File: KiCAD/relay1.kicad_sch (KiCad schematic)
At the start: 15 parts, among them K1 SANYOU_SRD_Form_C, K2 SANYOU_SRD_Form_C, Q2 UMH3N, Q3 MMBT3906, Q4 MMBT3906

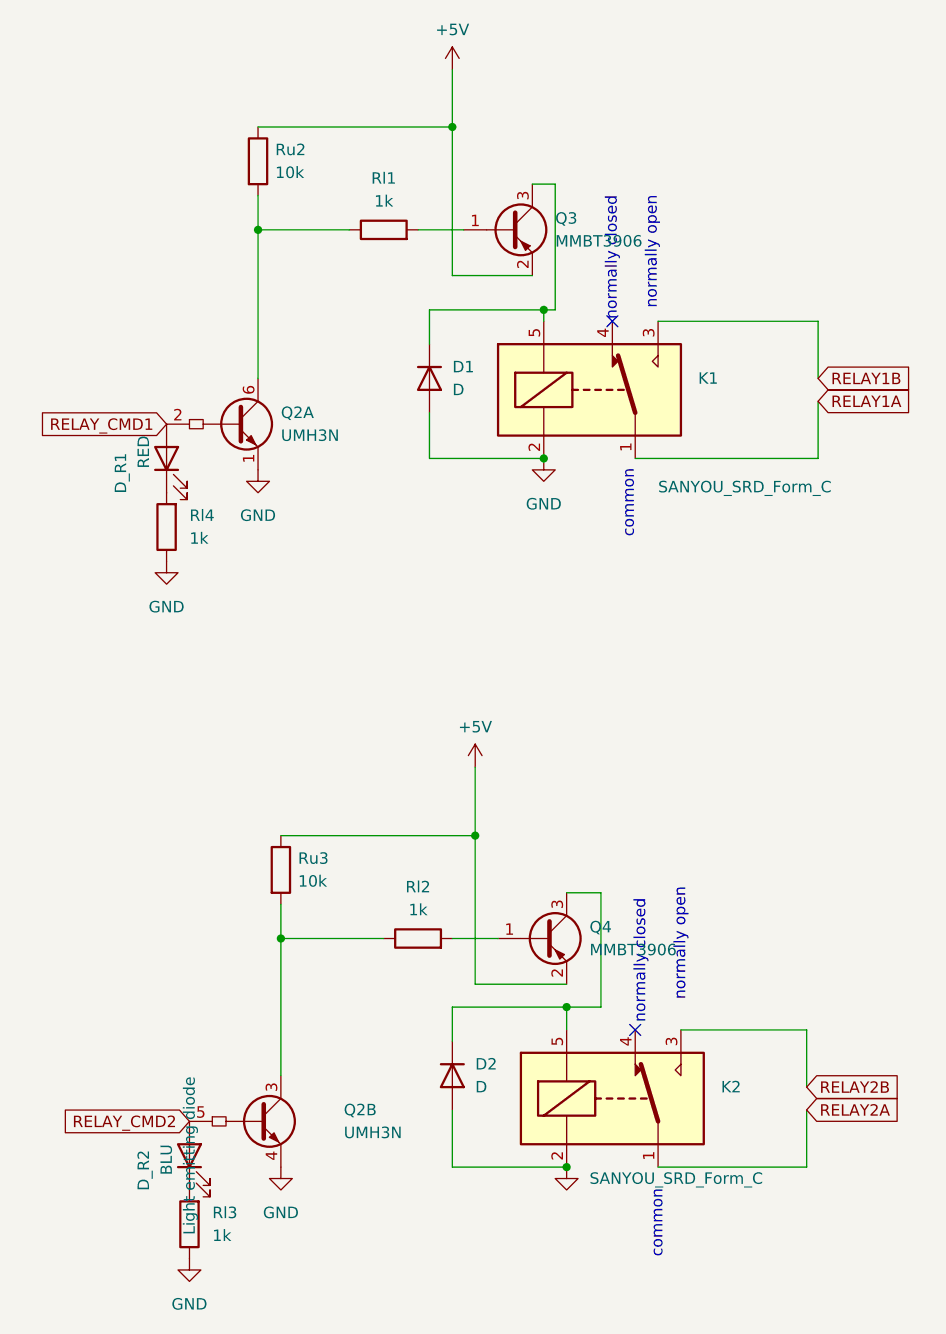
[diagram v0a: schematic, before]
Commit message: Version 2.1.0: four sonars, USB-C (#26)
## [2.1.0] - 2026-10-14

### Added
- **Hardware Board v3.1 & Enclosure Updates**: KiCAD PCB updates for
board v3.1 with revised BOM, updated 3D printable enclosure (better
SHTC3 thermal isolation, labeled connectors, improved USB-C port
clearance), and solder stencil support frame model.
- **HMM Visualization & Retraining Workflow**: Added
`analysis/hmm_to_svg.py` to generate SVG state transition diagrams from
trained HMM models, and added characterization workflow in
`analysis/retrain.py`.

### Changed
- **Sonar Watchdog & Timeout Stability**: Added sonar ping timeout
handling to prevent blocking pulses from triggering the ESP32 hardware
watchdog.

### Removed
- **Retired Legacy Hardware**: Removed firmware and PlatformIO
configuration support for legacy Classic ESP32 boards (Board v1/v2 /
`node32s`), focusing entirely on Board v3.x (ESP32-S3).

## [2.0.0] - 2026-08-21

### Added
- **Hardware Board v3.0 & ESP32-S3 Support**: Added PlatformIO
configuration (`usb_s3`), pin assignments for ESP32-S3, updated
schematic/PCB designs, and refreshed solder stencil fixture 3D models.
- **Quad-Sonar Support**: Integrated dual ultrasonic sensors per side (4
total) with updated state classification logic, training pipeline, and
retrained HMM models.
- **Home Assistant Probability Export**: Exported garage state
probabilities (`probOpen`, `probCar`, `probEmpty`) via Home Assistant
MQTT discovery.

### Changed
- **Svelte Build Tooling**: Pinned `svelteesp32` to v3.2.5 and updated
CI workflows to Node 22 for reproducible builds.
- **Dependency & Workflow Upgrades**: Upgraded `og3` to v0.6.3,
`og3x-oled` to v0.6.1, and updated GitHub Actions workflows to latest
versions.
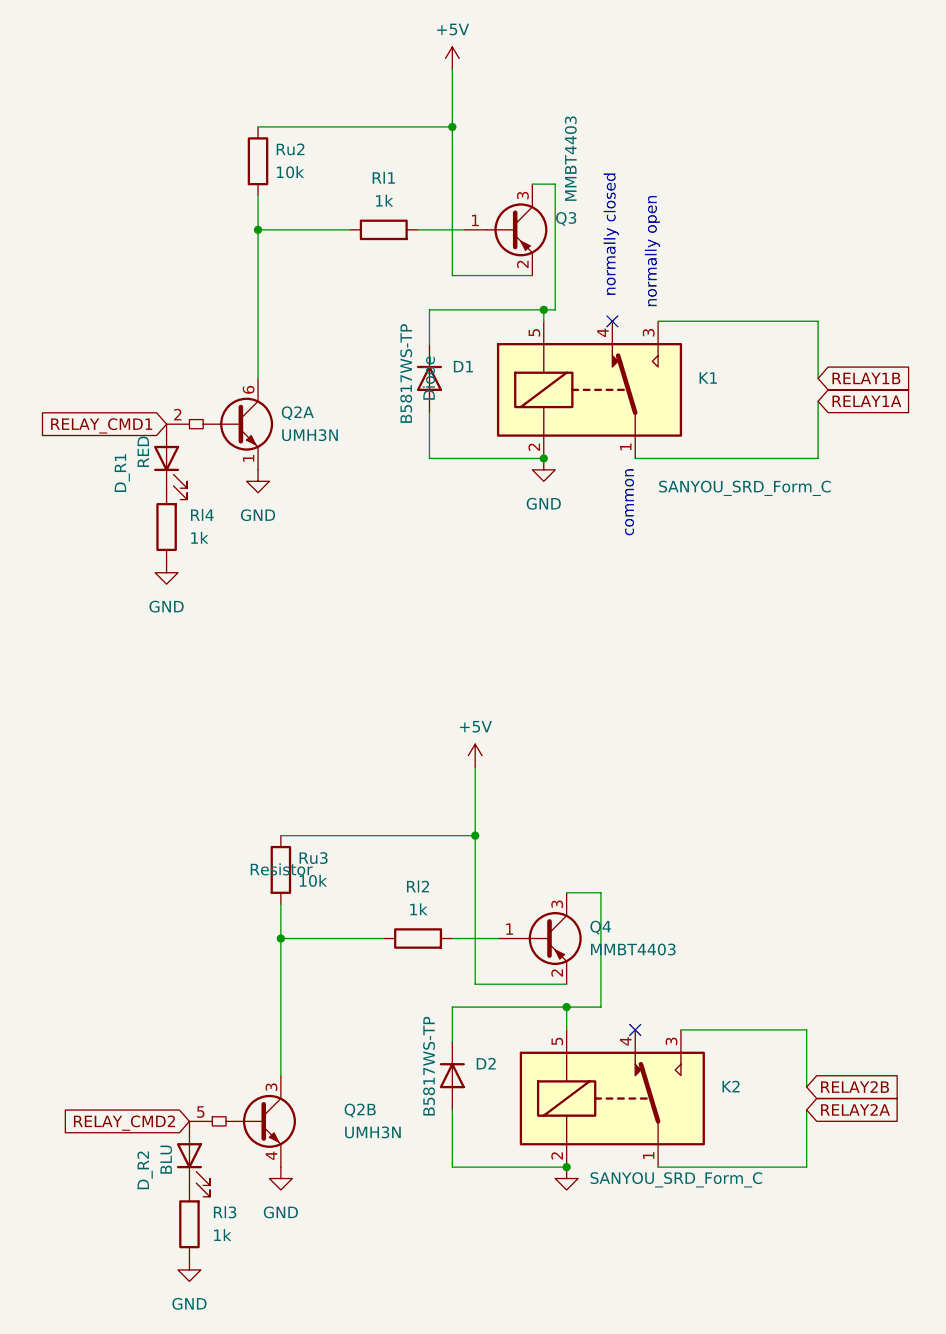
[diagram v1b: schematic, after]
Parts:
- D1, D2: value D -> B5817WS-TP
- Q3, Q4: value MMBT3906 -> MMBT4403
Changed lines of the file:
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@@
 	(text "normally closed"
 		(exclude_from_sim no)
-		(at 99.06 137.795 90)
+		(at 95.758 57.15 90)
 		(effects
 			(font
@@
 	(text "normally open"
 		(exclude_from_sim no)
-		(at 103.505 135.255 90)
-		(effects
-			(font
-				(size 1.27 1.27)
-			)
-			(justify left bottom)
-		)
-	)
-	(text "normally closed"
-		(exclude_from_sim no)
-		(at 95.885 59.69 90)
-		(effects
-			(font
-				(size 1.27 1.27)
-			)
-			(justify left bottom)
-		)
-	)
-	(text "normally open"
-		(exclude_from_sim no)
 		(at 100.33 58.42 90)
-		(effects
-			(font
-				(size 1.27 1.27)
-			)
-			(justify left bottom)
-		)
-	)
-	(text "common\n"
-		(exclude_from_sim no)
-		(at 100.965 163.83 90)
 		(effects
 			(font
@@
 		(dnp no)
 		(fields_autoplaced yes)
-		(property "Reference" "#PWR026"
+		(property "Reference" "#PWR0102"
 			(at 80.01 113.03 0)
 			(effects
@@
 			(project "Garage133"
 				(path "/42347524-93c6-40af-953e-da6b7c7bdf56/d90cc7d4-8419-4d79-8cad-11316efa8615"
-					(reference "#PWR026")
+					(reference "#PWR0102")
 					(unit 1)
 				)
@@
 			)
 		)
-		(property "Description" ""
+		(property "Description" "Sanyo SRD relay, Single Pole Miniature Power Relay,"
 			(at 95.25 146.05 0)
 			(effects
@@
 					(size 1.27 1.27)
 				)
+				(hide yes)
 			)
 		)
@@
 			)
 		)
-		(property "Description" ""
+		(property "Description" "Resistor"
 			(at 69.85 49.53 0)
 			(effects
@@
 					(size 1.27 1.27)
 				)
+				(hide yes)
 			)
 		)
@@
 			)
 		)
-		(property "Description" ""
+		(property "Description" "Sanyo SRD relay, Single Pole Miniature Power Relay,"
 			(at 92.71 67.31 0)
 			(effects
@@
 					(size 1.27 1.27)
 				)
+				(hide yes)
 			)
 		)
@@
 			)
 		)
-		(property "Value" "MMBT3906"
+		(property "Value" "MMBT4403"
 			(at 92.71 129.5399 0)
 			(effects
@@
 			)
 		)
-		(property "Description" ""
+		(property "Description" "Resistor"
 			(at 55.88 41.91 0)
 			(effects
@@
 					(size 1.27 1.27)
 				)
+				(hide yes)
 			)
 		)
@@
 		(on_board yes)
 		(dnp no)
-		(fields_autoplaced yes)
 		(property "Reference" "Q3"
 			(at 88.9 48.2599 0)
@@
 			)
 		)
-		(property "Value" "MMBT3906"
-			(at 88.9 50.7999 0)
+		(property "Value" "MMBT4403"
+			(at 90.678 46.482 90)
 			(effects
 				(font
@@
 			)
 		)
-		(property "Description" ""
+		(property "Description" "Resistor"
 			(at 58.42 120.65 0)
 			(effects
@@
 			)
 		)
-		(property "Description" ""
+		(property "Description" "Resistor"
 			(at 45.72 82.55 0)
 			(effects
@@
 					(size 1.27 1.27)
 				)
+				(hide yes)
 			)
 		)
@@
 		(dnp no)
 		(fields_autoplaced yes)
-		(property "Reference" "#PWR023"
+		(property "Reference" "#PWR0101"
 			(at 77.47 35.56 0)
 			(effects
@@
 			(project "Garage133"
 				(path "/42347524-93c6-40af-953e-da6b7c7bdf56/d90cc7d4-8419-4d79-8cad-11316efa8615"
-					(reference "#PWR023")
+					(reference "#PWR0101")
 					(unit 1)
 				)
@@
 			)
 		)
-		(property "Description" ""
+		(property "Description" "Resistor"
 			(at 73.66 128.27 0)
 			(effects
@@
 					(size 1.27 1.27)
 				)
+				(hide yes)
 			)
 		)
@@
 		(on_board yes)
 		(dnp no)
-		(fields_autoplaced yes)
 		(property "Reference" "D1"
 			(at 77.47 64.77 90)
@@
 			)
 		)
-		(property "Value" "D"
-			(at 77.47 67.31 90)
+		(property "Value" "B5817WS-TP"
+			(at 72.39 59.944 0)
 			(effects
 				(font
@@
 			)
 		)
-		(property "Description" ""
+		(property "Description" "Diode"
 			(at 74.93 66.04 0)
 			(effects
@@
 					(size 1.27 1.27)
 				)
+				(hide yes)
 			)
 		)
@@
 			)
 		)
-		(property "Description" ""
+		(property "Description" "Resistor"
 			(at 48.26 160.02 0)
 			(effects
@@
 					(size 1.27 1.27)
 				)
+				(hide yes)
 			)
 		)
@@
 		(on_board yes)
 		(dnp no)
-		(fields_autoplaced yes)
 		(property "Reference" "D2"
 			(at 80.01 142.24 90)
@@
 			)
 		)
-		(property "Value" "D"
-			(at 80.01 144.78 90)
+		(property "Value" "B5817WS-TP"
+			(at 74.93 136.906 0)
 			(effects
 				(font
@@
 			)
 		)
-		(property "Description" ""
+		(property "Description" "Diode"
 			(at 77.47 143.51 0)
 			(effects
@@
 					(size 1.27 1.27)
 				)
-			)
-		)
+				(hide yes)
+			)
+		)
